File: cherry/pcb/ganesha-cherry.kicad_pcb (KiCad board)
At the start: 2 copper layers, 275.5 x 124.6 mm, 204 parts, among them J1 MJ-4PP-9, J2 OLED, J3 MJ-4PP-9, J4 OLED, SW1 SW_PUSH, SW10 SW_PUSH, SW11 SW_PUSH, SW12 SW_PUSH, SW13 SW_PUSH, SW14 SW_PUSH, SW15 SW_PUSH, SW16 SW_PUSH, SW17 SW_PUSH, SW18 SW_PUSH, SW19 SW_PUSH, SW2 SW_PUSH, SW20 SW_PUSH, SW21 SW_PUSH, SW22 SW_PUSH, SW23 SW_PUSH, SW24 SW_PUSH, SW25 SW_PUSH, SW26 SW_PUSH, SW27 SW_PUSH, SW3 SW_PUSH, SW4 SW_PUSH, SW5 SW_PUSH, SW6 SW_PUSH, SW7 SW_PUSH, SW8 SW_PUSH, SW9 SW_PUSH, U1 ProMicro, U2 ProMicro

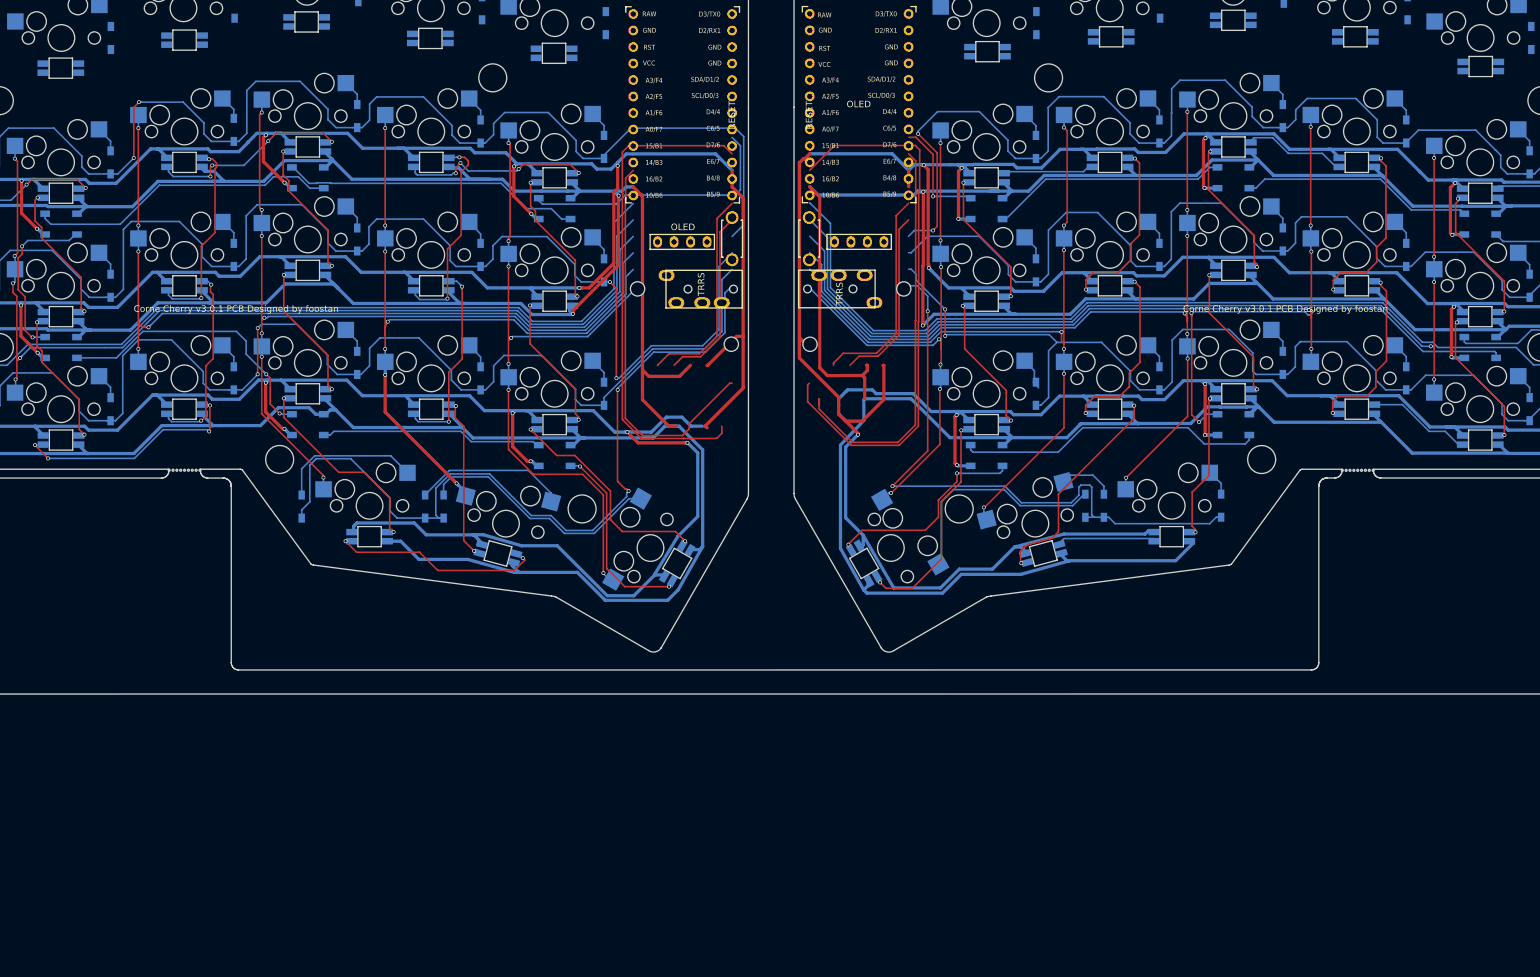
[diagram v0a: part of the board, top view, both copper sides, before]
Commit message: Layout Done, about to blow away previous tracks
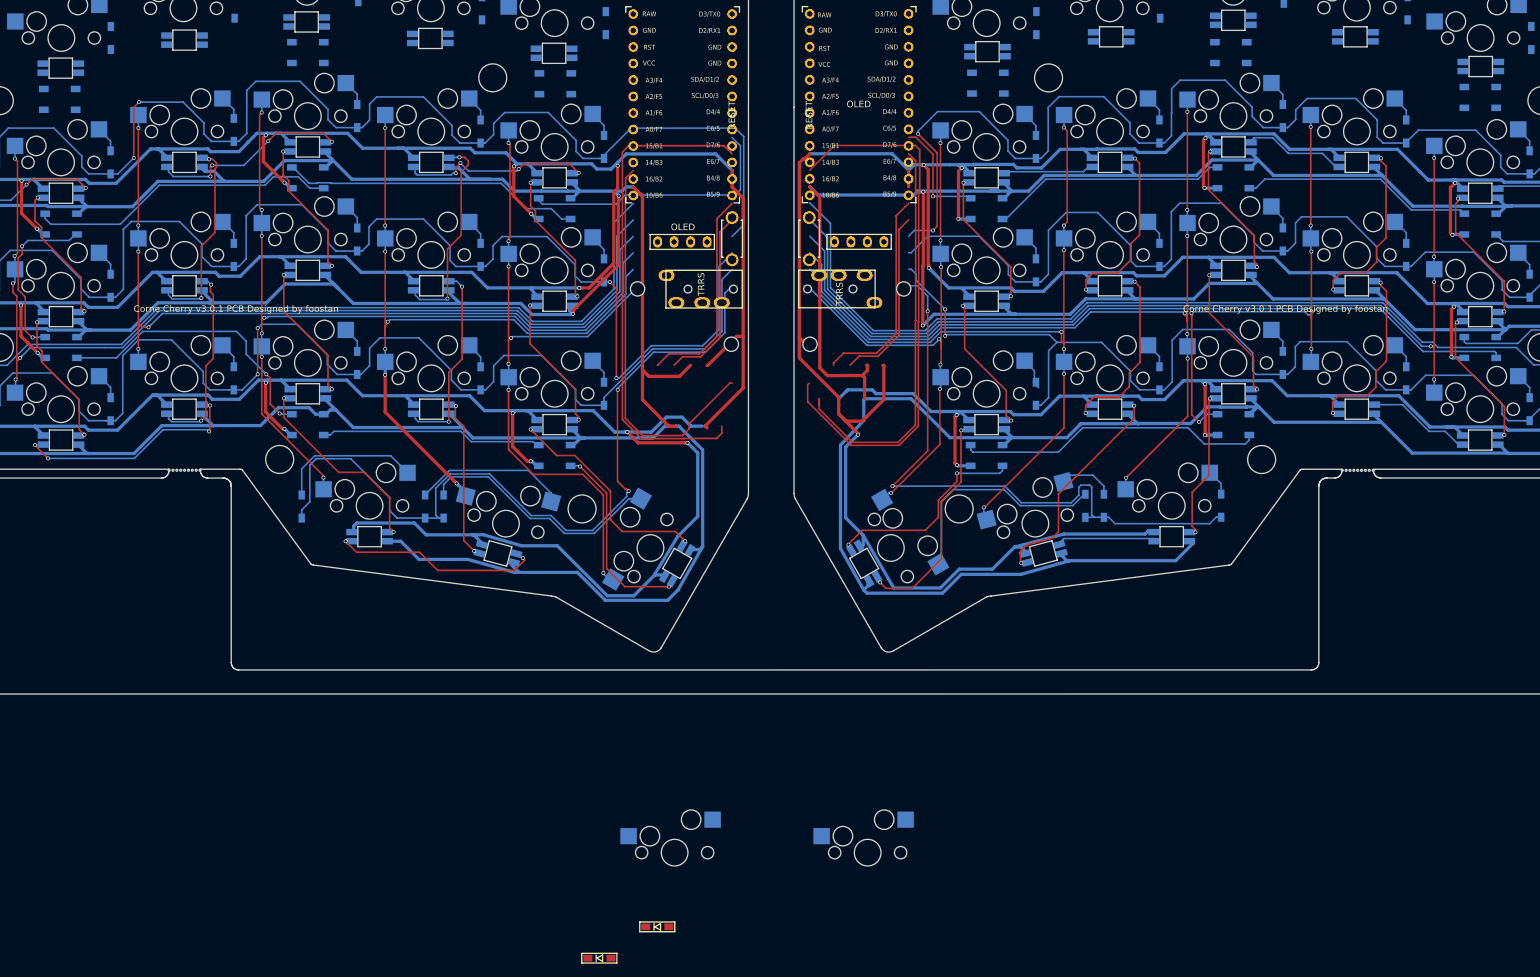
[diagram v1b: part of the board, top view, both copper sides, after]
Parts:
- removed the REF** at (115.0, 19.0)
- removed the REF** at (238.4, 16.4)
- removed the REF** at (257.7, 21.0)
- removed the REF** at (96.0, 16.7)
- removed the REF** at (76.9, 14.2)
- removed the REF** at (58.1, 17.0)
- removed the REF** at (39.1, 21.3)
- removed the REF** at (181.7, 18.7)
- removed the REF** at (200.8, 16.4)
- removed the REF** at (219.6, 13.9)
- added D28: D, kbd:D3_SMD_v2, F.Cu at (130.9, 153.5)
- added D_R28: D, kbd:D3_SMD_v2, F.Cu at (122.0, 158.3)
- added LED15: YS-SK6812MINI-E, kbd:YS-SK6812MINI-E, B.Cu at (76.9, 14.2)
- added LED16: YS-SK6812MINI-E, kbd:YS-SK6812MINI-E, B.Cu at (58.1, 17.0)
- added LED23: YS-SK6812MINI-E, kbd:YS-SK6812MINI-E, B.Cu at (39.1, 21.3)
- added LED5: YS-SK6812MINI-E, kbd:YS-SK6812MINI-E, B.Cu at (115.0, 19.0)
- added LED6: YS-SK6812MINI-E, kbd:YS-SK6812MINI-E, B.Cu at (96.0, 16.7)
- added LED_R_15: YS-SK6812MINI-E, kbd:YS-SK6812MINI-E, B.Cu at (219.6, 13.9)
- added LED_R_16: YS-SK6812MINI-E, kbd:YS-SK6812MINI-E, B.Cu at (238.4, 16.4)
- added LED_R_23: YS-SK6812MINI-E, kbd:YS-SK6812MINI-E, B.Cu at (257.7, 21.0)
- added LED_R_5: YS-SK6812MINI-E, kbd:YS-SK6812MINI-E, B.Cu at (181.7, 18.7)
- added LED_R_6: YS-SK6812MINI-E, kbd:YS-SK6812MINI-E, B.Cu at (200.8, 16.4)
- added LED_UR_1: WS2812B, LED_SMD:LED_WS2812B_PLCC4_5.0x5.0mm_P3.2mm, B.Cu at (257.6, 25.8)
- added LED_UR_2: WS2812B, LED_SMD:LED_WS2812B_PLCC4_5.0x5.0mm_P3.2mm, B.Cu at (219.2, 18.9)
- added LED_UR_3: WS2812B, LED_SMD:LED_WS2812B_PLCC4_5.0x5.0mm_P3.2mm, B.Cu at (181.8, 23.6)
- added LED_U_1: WS2812B, LED_SMD:LED_WS2812B_PLCC4_5.0x5.0mm_P3.2mm, B.Cu at (38.9, 26.1)
- added LED_U_2: WS2812B, LED_SMD:LED_WS2812B_PLCC4_5.0x5.0mm_P3.2mm, B.Cu at (77.1, 18.9)
- added LED_U_3: WS2812B, LED_SMD:LED_WS2812B_PLCC4_5.0x5.0mm_P3.2mm, B.Cu at (115.2, 23.7)
- added SW28: SW_PUSH, kbd:CherryMX_Hotswap_1.5u, F.Cu at (133.6, 142.1)
- added SW_R28: SW_PUSH, kbd:CherryMX_Hotswap_1.5u, F.Cu at (163.3, 142.1)
- renumbered D24 to D1, D4 to D10, D5 to D11, D6 to D12, D7 to D13, D8 to D14, D9 to D15, D10 to D16, D11 to D17, D12 to D18, D13 to D19, D24 to D2, D14 to D20, D15 to D21, D16 to D22, D17 to D23, D18 to D24, D19 to D25, D20 to D26, D21 to D27, D24 to D3, D24 to D4, D24 to D5, D24 to D6, D1 to D7, D2 to D8, D3 to D9, D24 to D_R1, D25 to D_R10, D26 to D_R11, D27 to D_R12, D28 to D_R13, D29 to D_R14, D30 to D_R15, D31 to D_R16, D32 to D_R17, D33 to D_R18, D34 to D_R19, D24 to D_R2, D35 to D_R20, D36 to D_R21, D37 to D_R22, D38 to D_R23, D39 to D_R24, D40 to D_R25, D41 to D_R26, D42 to D_R27, D24 to D_R3, D24 to D_R4, D24 to D_R5, D24 to D_R6, D22 to D_R7, D23 to D_R8, D24 to D_R9, LED27 to LED1, LED26 to LED10, LED25 to LED11, LED22 to LED12, LED16 to LED13, LED10 to LED14, LED9 to LED17, LED15 to LED18, LED21 to LED19, LED24 to LED2, LED14 to LED21, LED8 to LED22, REF** to LED24, LED7 to LED25, LED13 to LED26, LED19 to LED27, LED18 to LED3, LED12 to LED4, LED11 to LED7, LED17 to LED8, LED23 to LED9, LED54 to LED_R_1, LED53 to LED_R_10, LED52 to LED_R_11, LED49 to LED_R_12, LED43 to LED_R_13, LED37 to LED_R_14, LED36 to LED_R_17, LED42 to LED_R_18, LED48 to LED_R_19, LED51 to LED_R_2, LED47 to LED_R_20, LED41 to LED_R_21, LED35 to LED_R_22, REF** to LED_R_24, LED34 to LED_R_25, LED40 to LED_R_26, LED46 to LED_R_27, LED45 to LED_R_3, LED39 to LED_R_4, LED38 to LED_R_7, LED44 to LED_R_8, LED50 to LED_R_9, LED30 to LED_UR_4, LED29 to LED_UR_5, LED28 to LED_UR_6, LED31 to LED_UR_7, LED32 to LED_UR_8, LED33 to LED_UR_9, LED3 to LED_U_4, LED2 to LED_U_5, LED1 to LED_U_6, LED4 to LED_U_7, LED5 to LED_U_8, LED6 to LED_U_9, SWR1 to SW_R1, SWR10 to SW_R10, SWR11 to SW_R11, SWR12 to SW_R12, SWR13 to SW_R13, SWR14 to SW_R14, SWR15 to SW_R15, SWR16 to SW_R16, SWR17 to SW_R17, SWR18 to SW_R18, SWR19 to SW_R19, SWR2 to SW_R2, SWR20 to SW_R20, SWR21 to SW_R21, SWR22 to SW_R22, SWR23 to SW_R23, SWR24 to SW_R24, SWR25 to SW_R25, SWR26 to SW_R26, SWR27 to SW_R27, SWR3 to SW_R3, SWR4 to SW_R4, SWR5 to SW_R5, SWR6 to SW_R6, SWR7 to SW_R7, SWR8 to SW_R8, SWR9 to SW_R9
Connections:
- D1 pad 1: (no net) -> row0
- D1 pad 2: (no net) -> Net-(D1-Pad2)
- D10 pad 1: row0 -> row1
- D11 pad 1: row0 -> row1
- D12 pad 1: row0 -> row1
- D13 pad 1: row1 -> row2
- D14 pad 1: row1 -> row2
- D15 pad 1: row1 -> row2
- D16 pad 1: row1 -> row2
- D17 pad 1: row1 -> row2
- D18 pad 1: row1 -> row2
- D19 pad 1: row2 -> row3
- D2 pad 1: (no net) -> row0
- D2 pad 2: (no net) -> Net-(D2-Pad2)
- D20 pad 1: row2 -> row3
- D21 pad 1: row2 -> row3
- D22 pad 1: row2 -> row3
- D23 pad 1: row2 -> row3
- D24 pad 1: row2 -> row3
- D25 pad 1: row3 -> row4
- D26 pad 1: row3 -> row4
- D27 pad 1: row3 -> row4
- D3 pad 1: (no net) -> row0
- D3 pad 2: (no net) -> Net-(D3-Pad2)
- D4 pad 1: (no net) -> row0
- D4 pad 2: (no net) -> Net-(D4-Pad2)
- D5 pad 1: (no net) -> row0
- D5 pad 2: (no net) -> Net-(D5-Pad2)
- D6 pad 1: (no net) -> row0
- D6 pad 2: (no net) -> Net-(D6-Pad2)
- D7 pad 1: row0 -> row1
- D8 pad 1: row0 -> row1
- D9 pad 1: row0 -> row1
- D_R1 pad 1: (no net) -> row0_r
- D_R1 pad 2: (no net) -> Net-(D_R1-Pad2)
- D_R10 pad 1: row0_r -> row1_r
- D_R11 pad 1: row0_r -> row1_r
- D_R12 pad 1: row0_r -> row1_r
- D_R13 pad 1: row1_r -> row2_r
- D_R14 pad 1: row1_r -> row2_r
- D_R15 pad 1: row1_r -> row2_r
- D_R16 pad 1: row1_r -> row2_r
- D_R17 pad 1: row1_r -> row2_r
- D_R18 pad 1: row1_r -> row2_r
- D_R19 pad 1: row2_r -> row3_r
- D_R2 pad 1: (no net) -> row0_r
- D_R2 pad 2: (no net) -> Net-(D_R2-Pad2)
- D_R20 pad 1: row2_r -> row3_r
- D_R21 pad 1: row2_r -> row3_r
- D_R22 pad 1: row2_r -> row3_r
- D_R23 pad 1: row2_r -> row3_r
- D_R24 pad 1: row2_r -> row3_r
- D_R25 pad 1: row3_r -> row4_r
- D_R26 pad 1: row3_r -> row4_r
- D_R27 pad 1: row3_r -> row4_r
- D_R3 pad 1: (no net) -> row0_r
- D_R3 pad 2: (no net) -> Net-(D_R3-Pad2)
- D_R4 pad 1: (no net) -> row0_r
- D_R4 pad 2: (no net) -> Net-(D_R4-Pad2)
- D_R5 pad 1: (no net) -> row0_r
- D_R5 pad 2: (no net) -> Net-(D_R5-Pad2)
- D_R6 pad 1: (no net) -> row0_r
- D_R6 pad 2: (no net) -> Net-(D_R6-Pad2)
- D_R7 pad 1: row0_r -> row1_r
- D_R8 pad 1: row0_r -> row1_r
- D_R9 pad 1: row0_r -> row1_r
- LED14 pad 2: Net-(LED10-Pad2) (its old number) -> Net-(LED14-Pad2)
- LED17 pad 4: Net-(LED10-Pad2) (its old number) -> Net-(LED16-Pad2)
- LED22 pad 2: Net-(LED7-Pad4) -> Net-(LED22-Pad2)
- LED24 pad 1: (no net) -> VCC
- LED24 pad 2: (no net) -> Net-(LED24-Pad2)
- LED24 pad 3: (no net) -> GND
- LED24 pad 4: (no net) -> Net-(LED23-Pad2)
- LED25 pad 4: Net-(LED7-Pad4) -> Net-(LED24-Pad2)
- LED4 pad 2: Net-(LED11-Pad4) -> Net-(LED4-Pad2)
- LED7 pad 4: Net-(LED11-Pad4) -> Net-(LED6-Pad2)
- LED_R_1 pad 1: VDD -> VCC
- LED_R_1 pad 3: GNDA -> GND
- LED_R_10 pad 1: VDD -> VCC
- LED_R_10 pad 3: GNDA -> GND
- LED_R_11 pad 1: VDD -> VCC
- LED_R_11 pad 3: GNDA -> GND
- LED_R_12 pad 1: VDD -> VCC
- LED_R_12 pad 3: GNDA -> GND
- LED_R_13 pad 1: VDD -> VCC
- LED_R_13 pad 3: GNDA -> GND
- LED_R_14 pad 1: VDD -> VCC
- LED_R_14 pad 2: Net-(LED36-Pad4) -> Net-(LED_R_14-Pad2)
- LED_R_14 pad 3: GNDA -> GND
- LED_R_17 pad 1: VDD -> VCC
- LED_R_17 pad 3: GNDA -> GND
- LED_R_17 pad 4: Net-(LED36-Pad4) -> Net-(LED_R_16-Pad2)
- LED_R_18 pad 1: VDD -> VCC
- LED_R_18 pad 3: GNDA -> GND
- LED_R_19 pad 1: VDD -> VCC
- LED_R_19 pad 3: GNDA -> GND
- LED_R_2 pad 1: VDD -> VCC
- LED_R_2 pad 3: GNDA -> GND
- LED_R_20 pad 1: VDD -> VCC
- LED_R_20 pad 3: GNDA -> GND
- LED_R_21 pad 1: VDD -> VCC
- LED_R_21 pad 3: GNDA -> GND
- LED_R_22 pad 1: VDD -> VCC
- LED_R_22 pad 2: Net-(LED34-Pad4) -> Net-(LED_R_22-Pad2)
- LED_R_22 pad 3: GNDA -> GND
- LED_R_24 pad 1: (no net) -> VCC
- LED_R_24 pad 2: (no net) -> Net-(LED_R_24-Pad2)
- LED_R_24 pad 3: (no net) -> GND
- LED_R_24 pad 4: (no net) -> Net-(LED_R_23-Pad2)
- LED_R_25 pad 1: VDD -> VCC
- LED_R_25 pad 3: GNDA -> GND
- LED_R_25 pad 4: Net-(LED34-Pad4) -> Net-(LED_R_24-Pad2)
- LED_R_26 pad 1: VDD -> VCC
- LED_R_26 pad 3: GNDA -> GND
- LED_R_27 pad 1: VDD -> VCC
- LED_R_27 pad 3: GNDA -> GND
- LED_R_3 pad 1: VDD -> VCC
- LED_R_3 pad 3: GNDA -> GND
- LED_R_4 pad 1: VDD -> VCC
- LED_R_4 pad 2: Net-(LED38-Pad4) -> Net-(LED_R_4-Pad2)
- LED_R_4 pad 3: GNDA -> GND
- LED_R_7 pad 1: VDD -> VCC
- LED_R_7 pad 3: GNDA -> GND
- LED_R_7 pad 4: Net-(LED38-Pad4) -> Net-(LED_R_6-Pad2)
- LED_R_8 pad 1: VDD -> VCC
- LED_R_8 pad 3: GNDA -> GND
- LED_R_9 pad 1: VDD -> VCC
- LED_R_9 pad 3: GNDA -> GND
- LED_UR_4 pad 1: VDD -> VCC
- LED_UR_4 pad 3: GNDA -> GND
- LED_UR_4 pad 4: LED_r -> Net-(LED_UR_3-Pad2)
- LED_UR_5 pad 1: VDD -> VCC
- LED_UR_5 pad 3: GNDA -> GND
- LED_UR_6 pad 1: VDD -> VCC
- LED_UR_6 pad 3: GNDA -> GND
- LED_UR_7 pad 1: VDD -> VCC
- LED_UR_7 pad 3: GNDA -> GND
- LED_UR_8 pad 1: VDD -> VCC
- LED_UR_8 pad 3: GNDA -> GND
- LED_UR_9 pad 1: VDD -> VCC
- LED_UR_9 pad 3: GNDA -> GND
- LED_U_4 pad 4: LED -> Net-(LED_U_3-Pad2)
- SW1 pad 1: (no net) -> col0
- SW1 pad 2: (no net) -> Net-(D1-Pad2)
- SW2 pad 1: (no net) -> col1
- SW2 pad 2: (no net) -> Net-(D2-Pad2)
- SW25 pad 1: col3 -> col2
- SW26 pad 1: col4 -> col3
- SW27 pad 1: col5 -> col4
- SW3 pad 1: (no net) -> col2
- SW3 pad 2: (no net) -> Net-(D3-Pad2)
- SW4 pad 1: (no net) -> col3
- SW4 pad 2: (no net) -> Net-(D4-Pad2)
- SW5 pad 1: (no net) -> col4
- SW5 pad 2: (no net) -> Net-(D5-Pad2)
- SW6 pad 1: (no net) -> col5
- SW6 pad 2: (no net) -> Net-(D6-Pad2)
- SW_R1 pad 1: (no net) -> col0_r
- SW_R1 pad 2: (no net) -> Net-(D_R1-Pad2)
- SW_R2 pad 1: (no net) -> col1_r
- SW_R2 pad 2: (no net) -> Net-(D_R2-Pad2)
- SW_R25 pad 1: col3_r -> col2_r
- SW_R26 pad 1: col4_r -> col3_r
- SW_R27 pad 1: col5_r -> col4_r
- SW_R3 pad 1: (no net) -> col2_r
- SW_R3 pad 2: (no net) -> Net-(D_R3-Pad2)
- SW_R4 pad 1: (no net) -> col3_r
- SW_R4 pad 2: (no net) -> Net-(D_R4-Pad2)
- SW_R5 pad 1: (no net) -> col4_r
- SW_R5 pad 2: (no net) -> Net-(D_R5-Pad2)
- SW_R6 pad 1: (no net) -> col5_r
- SW_R6 pad 2: (no net) -> Net-(D_R6-Pad2)
- U1 pad 11: Net-(U1-Pad11) -> row4
- U2 pad 11: Net-(U2-Pad11) -> row4_r
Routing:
- net GNDA: track 615.3 -> 138.4 mm, vias 15 -> 1
- net GND: track 614.5 -> 1091.5 mm, vias 16 -> 30
- net VDD: track 573.1 -> 341.7 mm
- net VCC: track 544.3 -> 775.7 mm
- net row0_r: track 184.4 -> 0.00 mm, vias 2 -> 0
- net row4: track 0.00 -> 121.7 mm, vias 0 -> 2
- net row3: track 121.7 -> 0.00 mm, vias 2 -> 0
- net row4_r: track 0.00 -> 97.9 mm, vias 0 -> 2
- net row3_r: track 95.3 -> 172.6 mm
- net SDA: track 32.4 -> 0.00 mm
- net Net-(D28-Pad2): track 0.00 -> 32.4 mm
- net Net-(LED10-Pad2) (its old number): track 31.7 -> 0.00 mm, vias 4 -> 0
- net Net-(LED10-Pad2): track 33.5 -> 65.1 mm, vias 2 -> 6
- net row1_r: track 166.9 -> 184.4 mm, vias 0 -> 2
- net Net-(LED_UR_3-Pad2): track 0.00 -> 17.2 mm, vias 0 -> 1
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
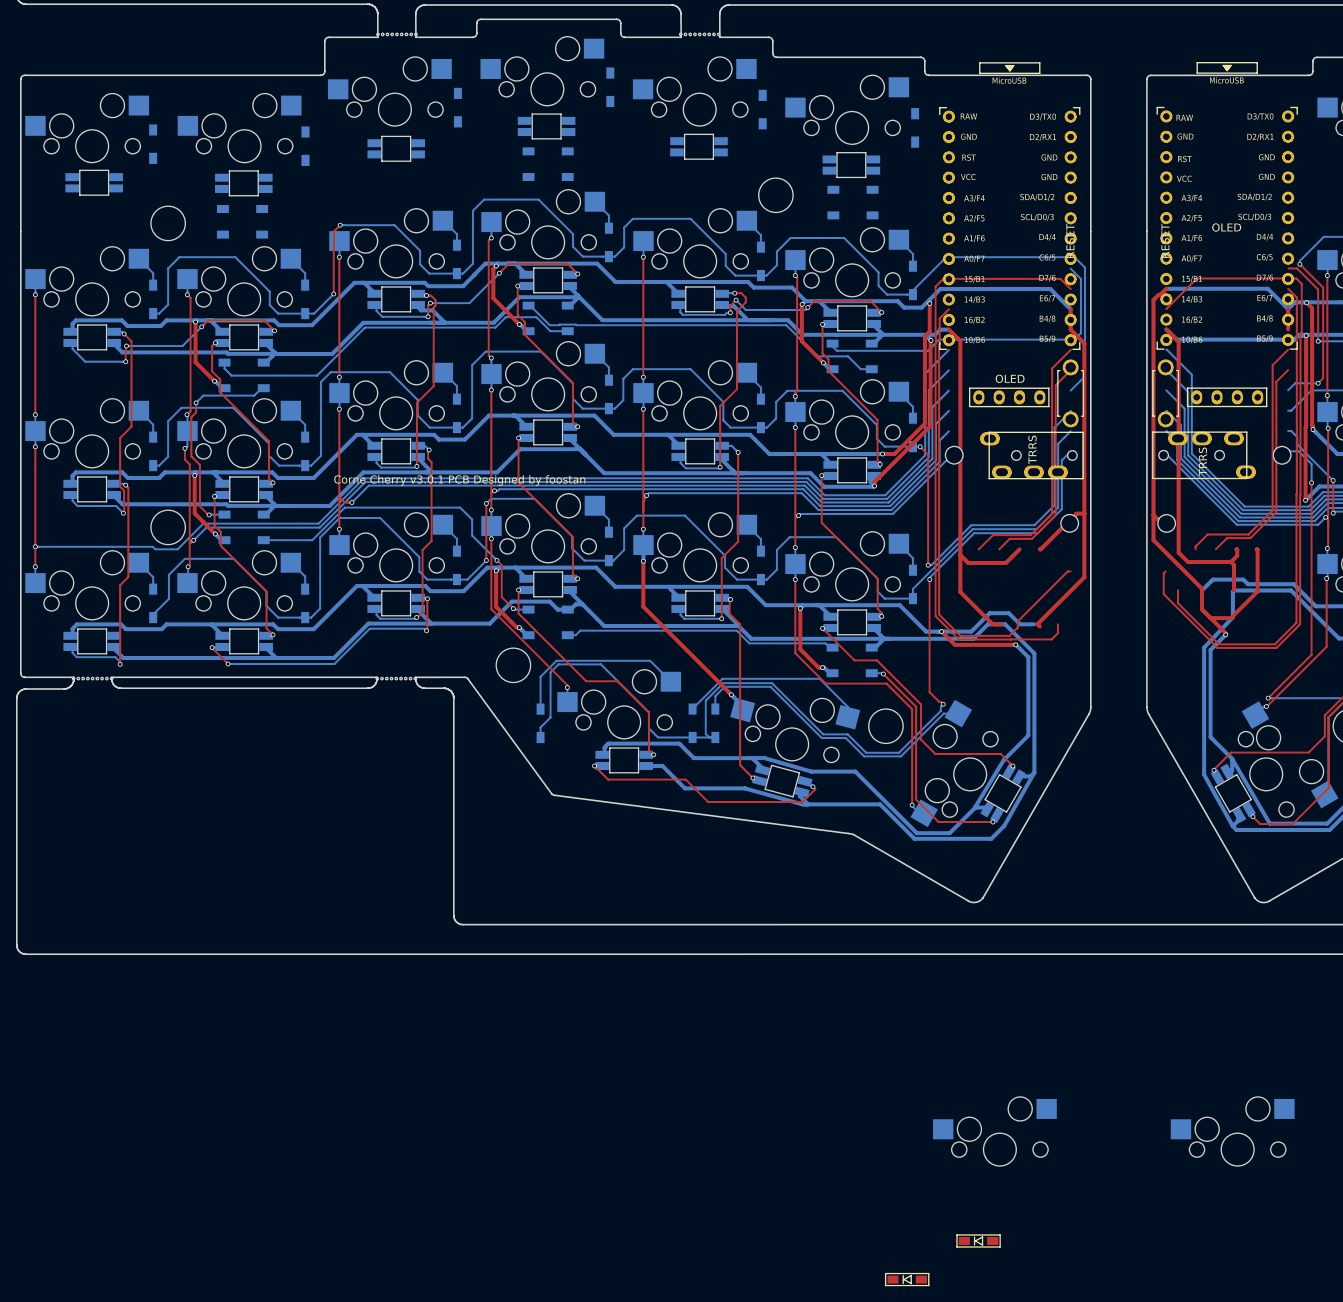
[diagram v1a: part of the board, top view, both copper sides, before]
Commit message: Left side tracks are routed! Need review.
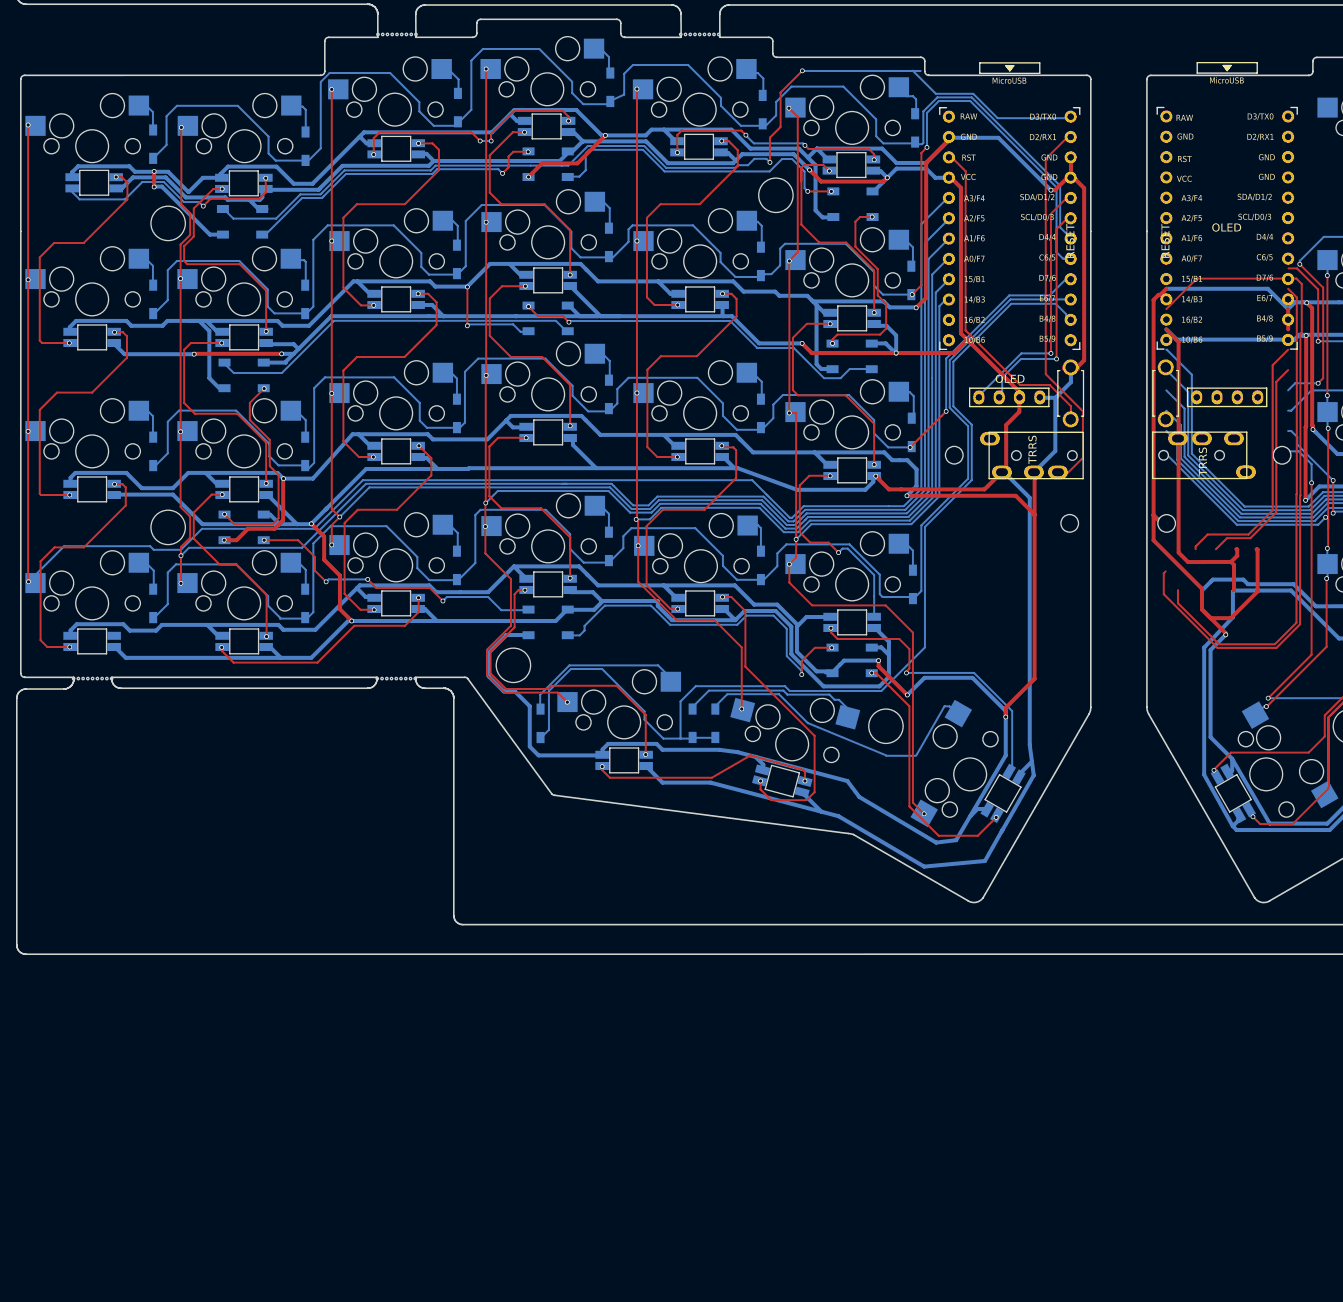
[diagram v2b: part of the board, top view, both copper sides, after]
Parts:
- removed D28, D_R28: D, kbd:D3_SMD_v2
- removed SW28, SW_R28: SW_PUSH, kbd:CherryMX_Hotswap_1.5u
- moved D12 0.20 mm to (122.5, 33.4)
- moved LED_U_3 0.20 mm to (115.2, 23.9)
- moved D18 0.15 mm to (122.6, 52.4)
- moved SW23 0.14 mm to (96.2, 69.1)
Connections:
- SW25 pad 1: col2 -> col3
- SW26 pad 1: col3 -> col4
- SW27 pad 1: col4 -> col5
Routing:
- net GND: track 1091.5 -> 1326.6 mm, vias 30 -> 28
- net row3: track 0.00 -> 190.5 mm
- net VCC: track 775.7 -> 920.2 mm, vias 2 -> 9
- net LED: track 41.1 -> 123.6 mm, vias 0 -> 2
- net col3: track 130.1 -> 180.6 mm, vias 7 -> 6
- net Net-(U1-Pad11): track 50.3 -> 0.00 mm
- net data: track 0.00 -> 45.9 mm
- net col1: track 149.4 -> 195.3 mm
- net col0: track 170.3 -> 215.6 mm, vias 5 -> 4
- net col2: track 125.8 -> 169.6 mm
- net col5: track 104.1 -> 147.5 mm, vias 7 -> 6
- net Net-(LED_U_2-Pad2): track 0.00 -> 40.1 mm, vias 0 -> 2
- net Net-(LED_U_1-Pad2): track 0.00 -> 38.7 mm, vias 0 -> 2
- net Net-(LED10-Pad2): track 65.1 -> 28.4 mm, vias 6 -> 2
- net Net-(LED16-Pad2): track 0.00 -> 33.3 mm, vias 0 -> 2
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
